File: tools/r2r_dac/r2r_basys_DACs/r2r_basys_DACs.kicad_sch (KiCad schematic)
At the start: 38 parts

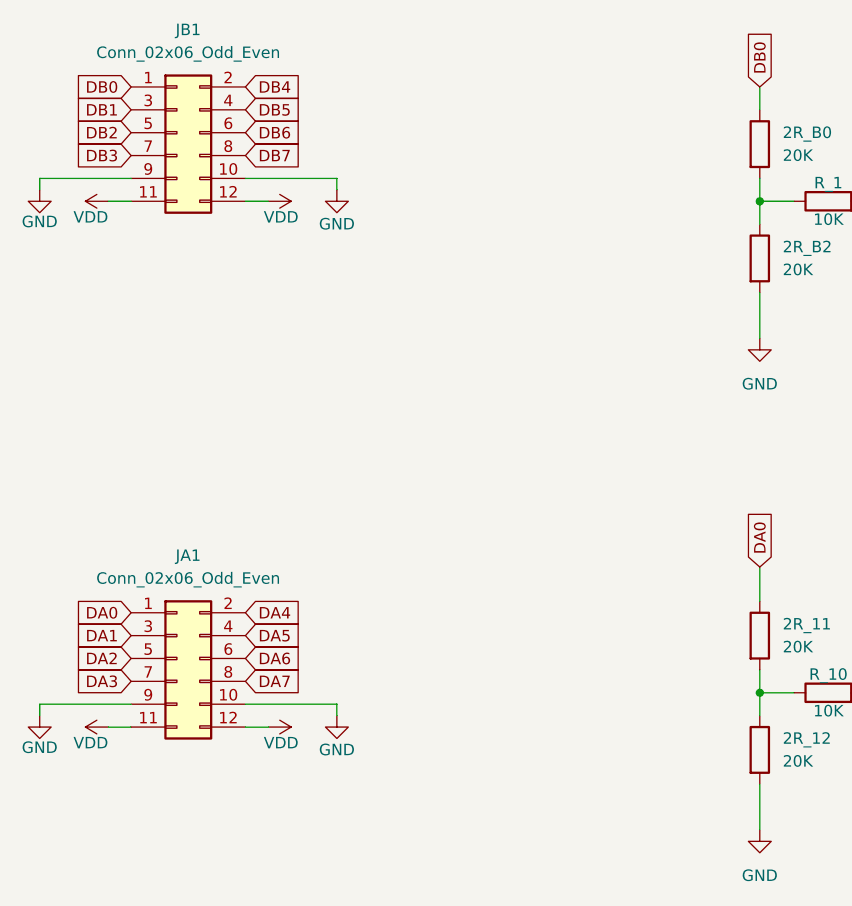
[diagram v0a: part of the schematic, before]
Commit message: r2r dac + some fixes to final game - now it semiworks
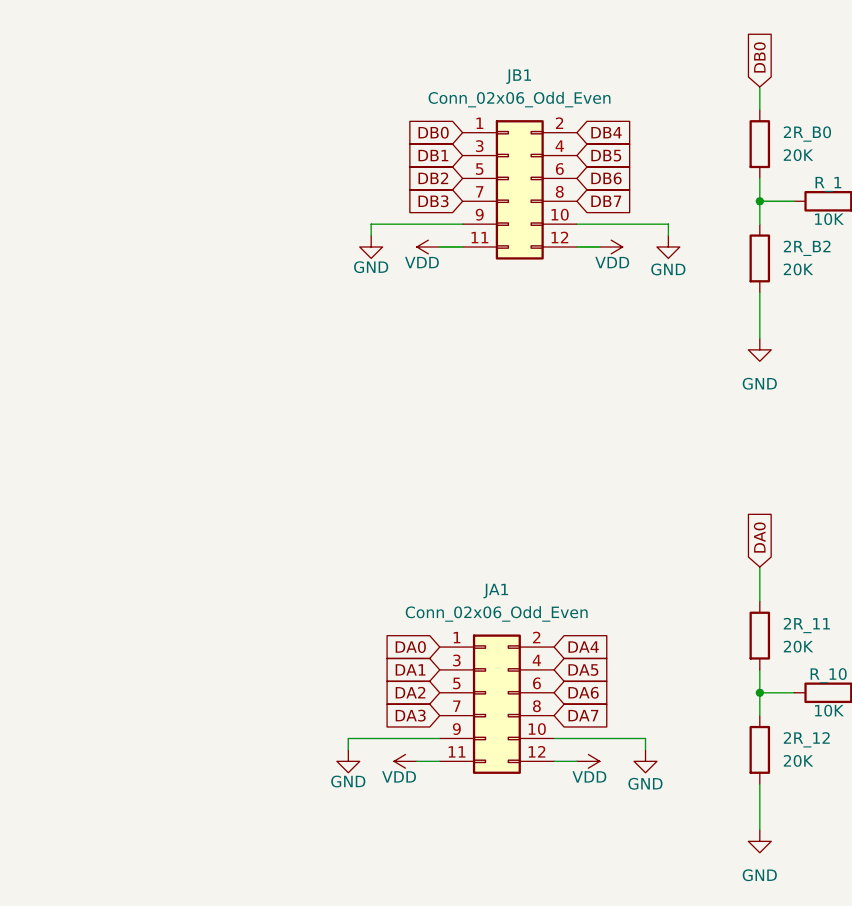
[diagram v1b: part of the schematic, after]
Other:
- moved on the sheet: JA1, JB1
